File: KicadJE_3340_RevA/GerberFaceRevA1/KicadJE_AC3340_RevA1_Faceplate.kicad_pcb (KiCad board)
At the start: 2 copper layers, 40 x 128 mm, 20 parts

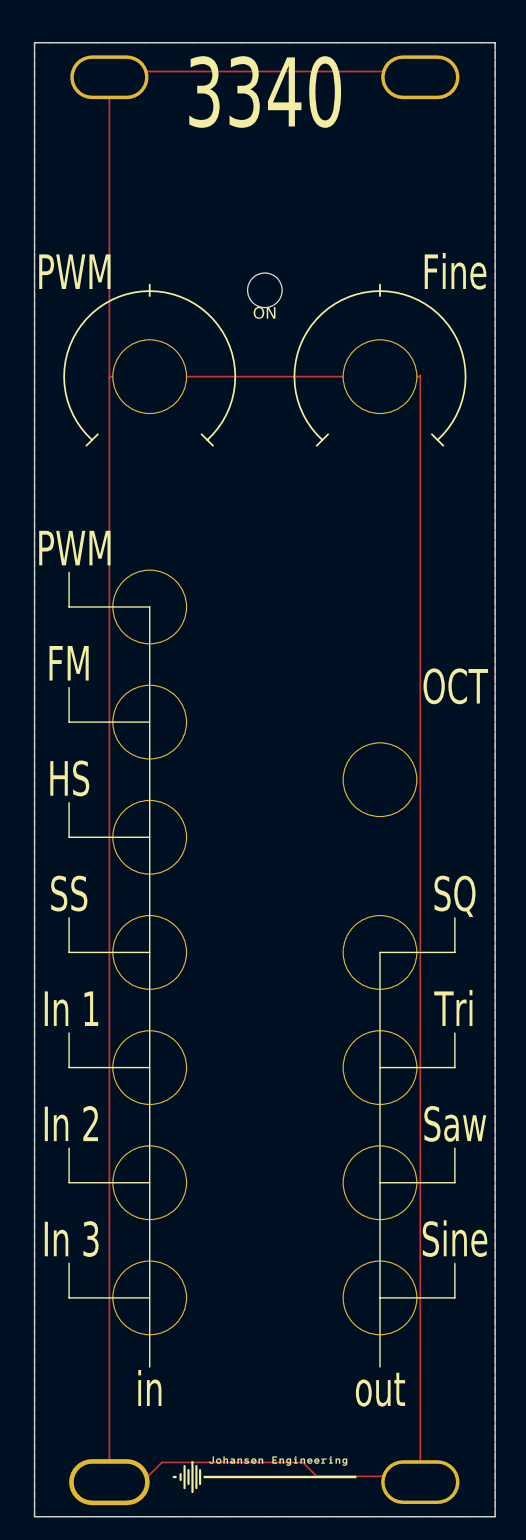
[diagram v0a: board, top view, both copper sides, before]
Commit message: Faceplate A2
change order of inputs
move octave
move led hole
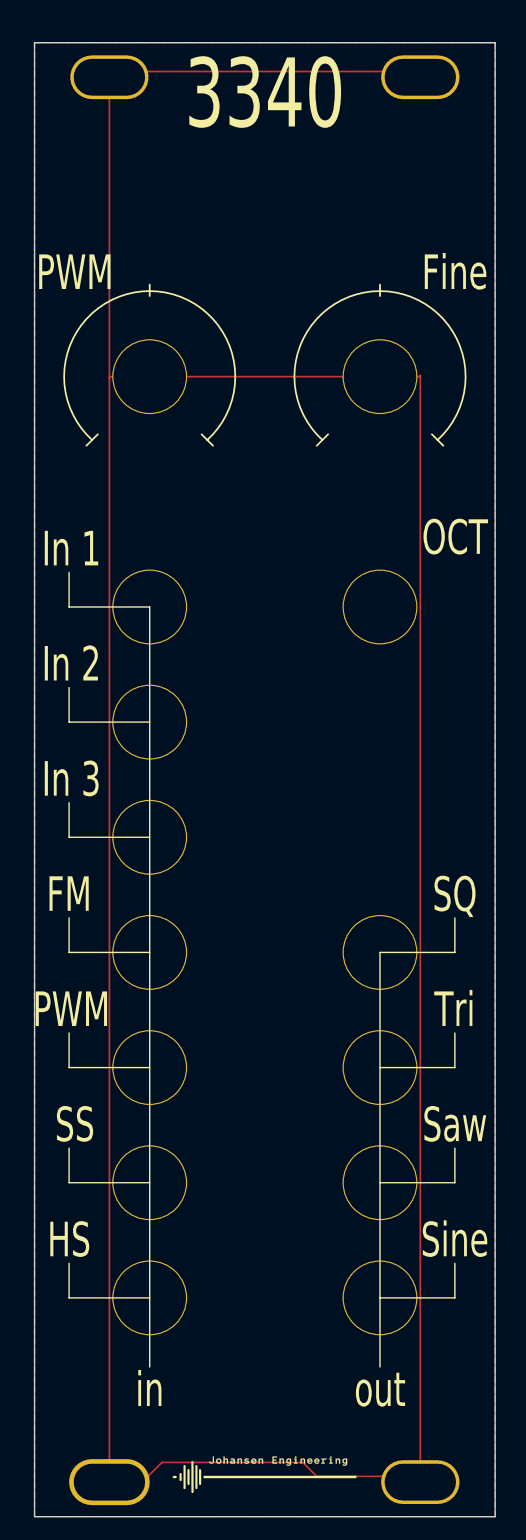
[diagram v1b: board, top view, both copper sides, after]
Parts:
- removed TP114: ON, AJ:LED_Hole_3mm
- moved REF** 15.0 mm to (-20.0, 85.0)
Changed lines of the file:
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@@
     (tracks 14)
     (zones 0)
-    (modules 20)
+    (modules 19)
     (nets 2)
   )
@@
     (solder_mask_min_width 0.25)
     (aux_axis_origin 0 0)
-    (visible_elements 7FFFFFFF)
+    (visible_elements 7FFFF7FF)
     (pcbplotparams
       (layerselection 0x010fc_ffffffff)
@@
     (uvia_drill 0.1)
     (add_net GND)
-  )
-  (module AJ:LED_Hole_3mm (layer F.Cu)
-    (at -30 57.5)
-    (descr "Mounting Hole 2.5mm, no annular")
-    (tags "mounting hole 2.5mm no annular")
-    (attr virtual)
-    (fp_text reference TP114 (at 0 -1.75) (layer F.Fab)
-      (effects (font (size 1 1) (thickness 0.15)))
-    )
-    (fp_text value ON (at 0 2) (layer F.SilkS)
-      (effects (font (size 1 1) (thickness 0.15)))
-    )
-    (fp_circle (center 0 0) (end 2.75 0) (layer F.CrtYd) (width 0.05))
-    (fp_circle (center 0 0) (end 2.5 0) (layer Cmts.User) (width 0.15))
-    (fp_text user %R (at 0 -1) (layer F.Fab)
-      (effects (font (size 1 1) (thickness 0.15)))
-    )
-    (pad "" np_thru_hole circle (at 0 0) (size 3 3) (drill 3) (layers *.Cu *.Mask))
   )
   (module AJ:MountingHole_Eurorack3 (layer F.Cu)
@@
   )
   (module AJ:Pot_6m3 (layer F.Cu)
-    (at -20 100)
+    (at -20 85)
     (descr "Mounting Hole 6.5mm, no annular")
     (tags "mounting hole 6.5mm no annular")
@@
     (effects (font (size 1.3 1.2) (thickness 0.3)) (justify left mirror))
   )
-  (gr_text Pot_6m3 (at -16.5 94.5) (layer B.SilkS)
+  (gr_text Pot_6m3 (at -15.6 89.8) (layer B.SilkS)
     (effects (font (size 1.3 1.2) (thickness 0.3)) (justify left mirror))
   )
@@
   (gr_line (start -47 145) (end -47 142) (layer F.SilkS) (width 0.12))
   (gr_line (start -40 145) (end -47 145) (layer F.SilkS) (width 0.12))
-  (gr_line (start -47 95) (end -47 92) (layer F.SilkS) (width 0.12))
+  (gr_line (start -47 135) (end -47 132) (layer F.SilkS) (width 0.12))
   (gr_line (start -40 135) (end -47 135) (layer F.SilkS) (width 0.12))
-  (gr_line (start -47 85) (end -47 82) (layer F.SilkS) (width 0.12))
+  (gr_line (start -47 125) (end -47 122) (layer F.SilkS) (width 0.12))
   (gr_line (start -40 125) (end -47 125) (layer F.SilkS) (width 0.12))
   (gr_line (start -40 115) (end -47 115) (layer F.SilkS) (width 0.12))
@@
   (gr_line (start -40 105) (end -47 105) (layer F.SilkS) (width 0.12))
   (gr_line (start -47 105) (end -47 102) (layer F.SilkS) (width 0.12))
-  (gr_line (start -47 135) (end -47 132) (layer F.SilkS) (width 0.12))
+  (gr_line (start -47 95) (end -47 92) (layer F.SilkS) (width 0.12))
   (gr_line (start -40 95) (end -47 95) (layer F.SilkS) (width 0.12))
-  (gr_line (start -47 125) (end -47 122) (layer F.SilkS) (width 0.12))
+  (gr_line (start -47 85) (end -47 82) (layer F.SilkS) (width 0.12))
   (gr_line (start -40 85) (end -47 85) (layer F.SilkS) (width 0.12))
-  (gr_text PWM (at -46.5 80) (layer F.SilkS)
-    (effects (font (size 3 2) (thickness 0.5)))
-  )
-  (gr_text SS (at -47 110) (layer F.SilkS)
-    (effects (font (size 3 2) (thickness 0.5)))
-  )
-  (gr_text HS (at -47 100) (layer F.SilkS)
-    (effects (font (size 3 2) (thickness 0.5)))
-  )
-  (gr_text "In 1" (at -46.8 120) (layer F.SilkS)
-    (effects (font (size 3 2) (thickness 0.5)))
-  )
-  (gr_text "In 2" (at -46.8 130) (layer F.SilkS)
-    (effects (font (size 3 2) (thickness 0.5)))
-  )
-  (gr_text "In 3" (at -46.8 140) (layer F.SilkS)
-    (effects (font (size 3 2) (thickness 0.5)))
-  )
-  (gr_text FM (at -47 90) (layer F.SilkS)
+  (gr_text PWM (at -46.8 120) (layer F.SilkS)
+    (effects (font (size 3 2) (thickness 0.5)))
+  )
+  (gr_text SS (at -46.5 130) (layer F.SilkS)
+    (effects (font (size 3 2) (thickness 0.5)))
+  )
+  (gr_text HS (at -47 140) (layer F.SilkS)
+    (effects (font (size 3 2) (thickness 0.5)))
+  )
+  (gr_text "In 1" (at -46.8 80) (layer F.SilkS)
+    (effects (font (size 3 2) (thickness 0.5)))
+  )
+  (gr_text "In 2" (at -46.8 90) (layer F.SilkS)
+    (effects (font (size 3 2) (thickness 0.5)))
+  )
+  (gr_text "In 3" (at -46.8 100) (layer F.SilkS)
+    (effects (font (size 3 2) (thickness 0.5)))
+  )
+  (gr_text FM (at -47 110) (layer F.SilkS)
     (effects (font (size 3 2) (thickness 0.5)))
   )
@@
     (effects (font (size 3 2) (thickness 0.5)))
   )
-  (gr_text OCT (at -13.5 92) (layer F.SilkS)
-    (effects (font (size 3 2) (thickness 0.5)))
-  )
+  (gr_text OCT (at -13.5 79) (layer F.SilkS)
+    (effects (font (size 3 2) (thickness 0.5)))
+  )
